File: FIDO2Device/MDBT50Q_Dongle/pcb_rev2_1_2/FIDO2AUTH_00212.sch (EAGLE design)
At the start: 39 parts, among them CN1 TE-1734028, CN2 IF_4PIN, CN5 IF_2PIN_SOL, SW1 SKRPACE010, SW2 SKTADAE010, U1 MDBT50Q-P1M, U2 XC6206P332MR-G, U3 ATECC608A-MAHDA-S, X1 NX3215SA-32.768K

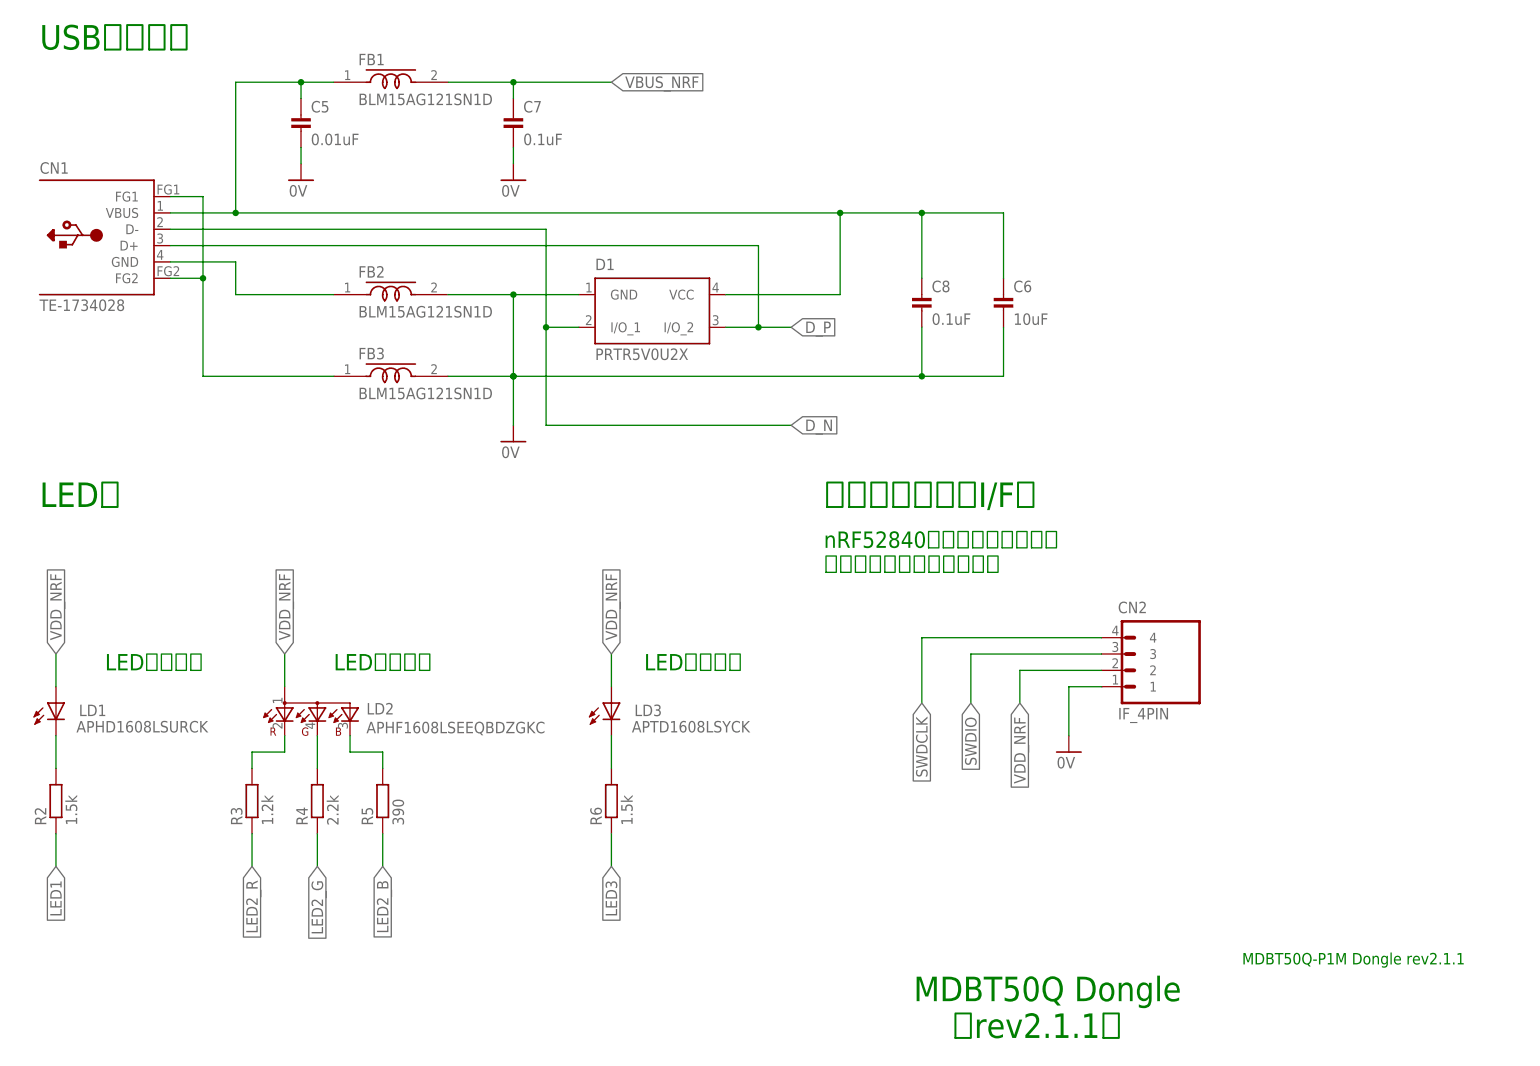
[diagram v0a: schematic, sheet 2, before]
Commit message: 回路図・レイアウトを修正
・３色LEDを単色LEDに分割
・LEDの部品番号を修正
・旧・LED1（赤色LED）は廃止
・配線／ビア位置を若干見直し
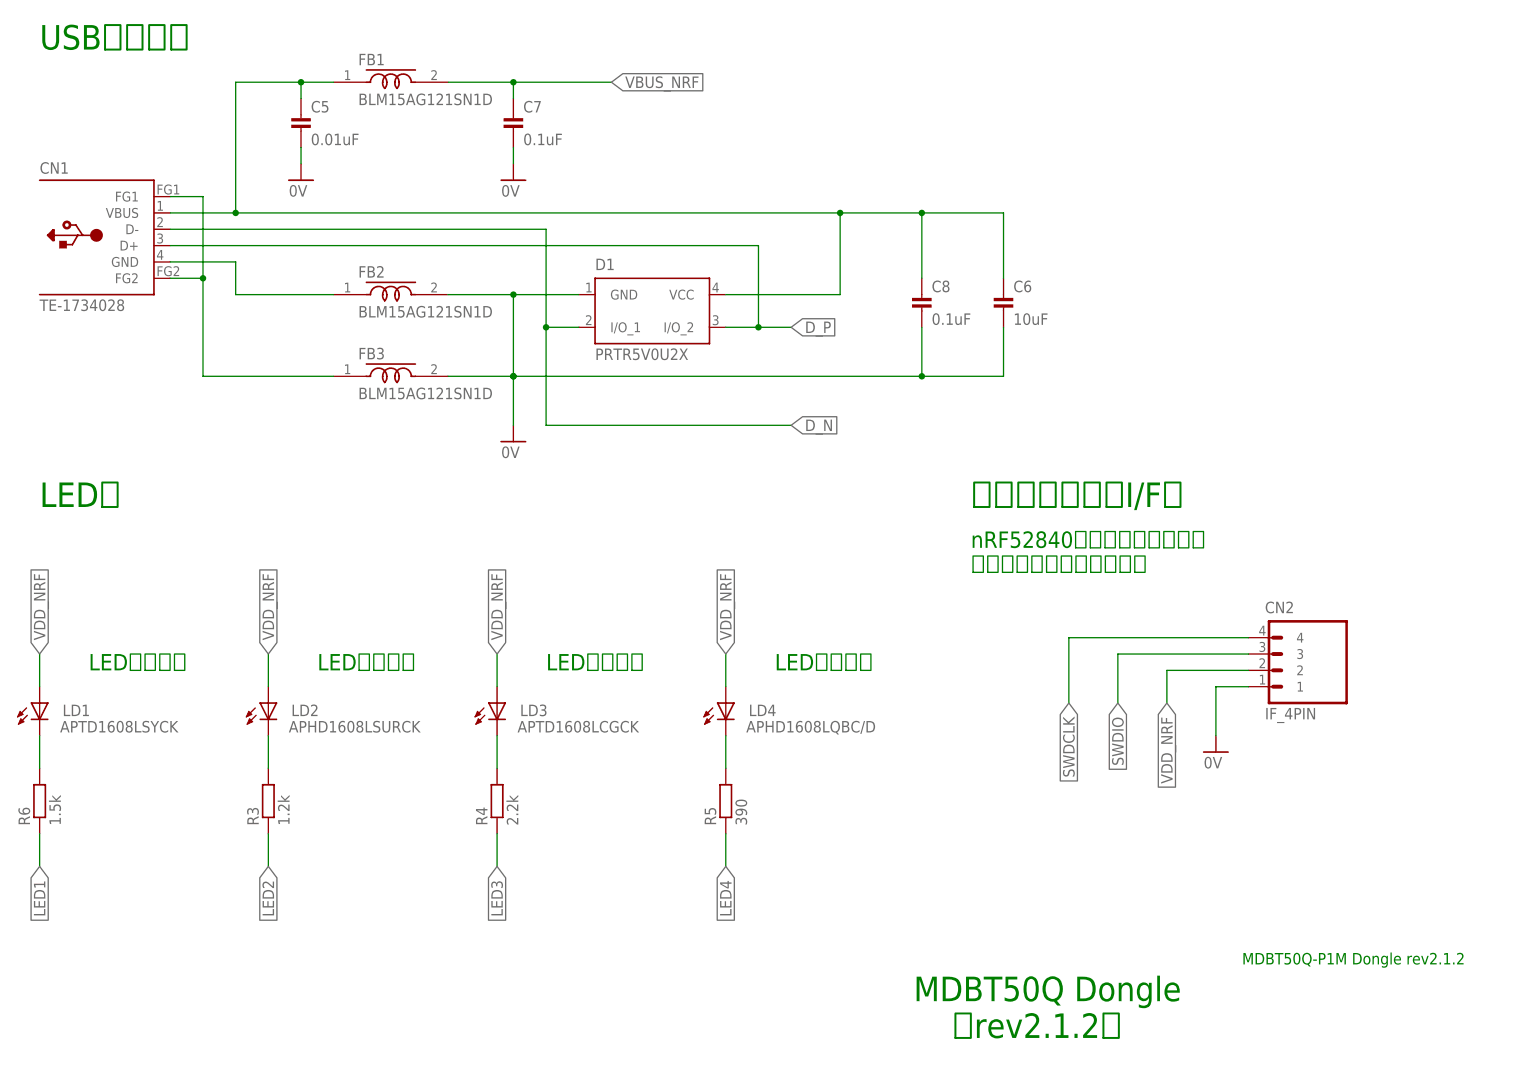
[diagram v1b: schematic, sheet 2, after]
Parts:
- removed R2: 1.5k, Parts:RESISTOR_0402
- added LD4: APHD1608LQBC/D, Parts:APHD1608LQBC/D
- LD1: value APHD1608LSURCK -> APTD1608LSYCK; device Parts:APHD1608LSURCK -> Parts:APTD1608LSYCK
- LD2: value APHF1608LSEEQBDZGKC -> APHD1608LSURCK; device Parts:APHF1608LSEEQBDZGKC -> Parts:APHD1608LSURCK
- LD3: value APTD1608LSYCK -> APTD1608LCGCK; device Parts:APTD1608LSYCK -> Parts:APTD1608LCGCK
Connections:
- net LED2_B renamed LED4
- net LED2_R renamed LED2
- removed net LED2_G: R4.1, U1.P1.09
- removed net N$11: LD1.C, R2.2
- net LED1: now also R6.1, U1.P0.26; no longer R2.1, U1.P0.27
- net LED3: now also R4.1, U1.P1.09; no longer R6.1, U1.P0.26
- net N$1: now also LD4.C, R5.2; no longer LD2.CRED, R3.2
- net N$6: now also LD3.C; no longer LD2.CGREEN
- net N$7: now also LD2.C, R3.2; no longer LD2.CBLUE, R5.2
- net N$8: now also LD1.C; no longer LD3.C
- net VDD_NRF: now also LD4.A
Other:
- note added: "LED（緑色）"
- note added: "LED（青色）"
- note added: "MDBT50Q Dongle （rev2.1.2）"
- note added: "MDBT50Q-P1M Dongle rev2.1.2"
- note removed: "LED（３色）"
- note removed: "MDBT50Q Dongle （rev2.1.1）"
- note removed: "MDBT50Q-P1M Dongle rev2.1.1"
- moved on the sheet: CN2, LD1, LD3, R3, R4, R5, R6

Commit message: 回路図・レイアウトを修正
・LED品番を、入手性の良い物に変更
・LED関連のレイアウトを修正（パターンを修正）
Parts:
- LD1: value APTD1608LSYCK -> APTD1608LSECK/J4-PF; device Parts:APTD1608LSYCK -> Parts:APTD1608LSECK/J4-PF
- LD3: value APTD1608LCGCK -> APTD1608LZGCK; device Parts:APTD1608LCGCK -> Parts:APTD1608LZGCK
- LD4: value APHD1608LQBC/D -> APTD1608LVBC/D; device Parts:APHD1608LQBC/D -> Parts:APTD1608LVBC/D
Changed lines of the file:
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@@
 <grid distance="0.1" unitdist="inch" unit="inch" style="lines" multiple="1" display="yes" altdistance="0.01" altunitdist="inch" altunit="inch"/>
 <layers>
-<layer number="1" name="Top" color="4" fill="1" visible="no" active="no"/>
-<layer number="2" name="Route2" color="1" fill="3" visible="no" active="no"/>
-<layer number="3" name="Route3" color="4" fill="3" visible="no" active="no"/>
-<layer number="14" name="Route14" color="1" fill="6" visible="no" active="no"/>
-<layer number="15" name="Route15" color="4" fill="6" visible="no" active="no"/>
-<layer number="16" name="Bottom" color="1" fill="1" visible="no" active="no"/>
-<layer number="17" name="Pads" color="2" fill="1" visible="no" active="no"/>
-<layer number="18" name="Vias" color="2" fill="1" visible="no" active="no"/>
-<layer number="19" name="Unrouted" color="6" fill="1" visible="no" active="no"/>
-<layer number="20" name="Dimension" color="15" fill="1" visible="no" active="no"/>
-<layer number="21" name="tPlace" color="7" fill="1" visible="no" active="no"/>
-<layer number="22" name="bPlace" color="7" fill="1" visible="no" active="no"/>
-<layer number="23" name="tOrigins" color="15" fill="1" visible="no" active="no"/>
-<layer number="24" name="bOrigins" color="15" fill="1" visible="no" active="no"/>
-<layer number="25" name="tNames" color="7" fill="1" visible="no" active="no"/>
-<layer number="26" name="bNames" color="7" fill="1" visible="no" active="no"/>
-<layer number="27" name="tValues" color="7" fill="1" visible="no" active="no"/>
-<layer number="28" name="bValues" color="7" fill="1" visible="no" active="no"/>
+<layer number="1" name="Top" color="4" fill="1" visible="yes" active="no"/>
+<layer number="2" name="Route2" color="1" fill="3" visible="yes" active="no"/>
+<layer number="3" name="Route3" color="4" fill="3" visible="yes" active="no"/>
+<layer number="14" name="Route14" color="1" fill="6" visible="yes" active="no"/>
+<layer number="15" name="Route15" color="4" fill="6" visible="yes" active="no"/>
+<layer number="16" name="Bottom" color="1" fill="1" visible="yes" active="no"/>
+<layer number="17" name="Pads" color="2" fill="1" visible="yes" active="no"/>
+<layer number="18" name="Vias" color="2" fill="1" visible="yes" active="no"/>
+<layer number="19" name="Unrouted" color="6" fill="1" visible="yes" active="no"/>
+<layer number="20" name="Dimension" color="15" fill="1" visible="yes" active="no"/>
+<layer number="21" name="tPlace" color="7" fill="1" visible="yes" active="no"/>
+<layer number="22" name="bPlace" color="7" fill="1" visible="yes" active="no"/>
+<layer number="23" name="tOrigins" color="15" fill="1" visible="yes" active="no"/>
+<layer number="24" name="bOrigins" color="15" fill="1" visible="yes" active="no"/>
+<layer number="25" name="tNames" color="7" fill="1" visible="yes" active="no"/>
+<layer number="26" name="bNames" color="7" fill="1" visible="yes" active="no"/>
+<layer number="27" name="tValues" color="7" fill="1" visible="yes" active="no"/>
+<layer number="28" name="bValues" color="7" fill="1" visible="yes" active="no"/>
 <layer number="29" name="tStop" color="7" fill="3" visible="no" active="no"/>
 <layer number="30" name="bStop" color="7" fill="6" visible="no" active="no"/>
@@
 <layer number="35" name="tGlue" color="7" fill="4" visible="no" active="no"/>
 <layer number="36" name="bGlue" color="7" fill="5" visible="no" active="no"/>
-<layer number="37" name="tTest" color="7" fill="1" visible="no" active="no"/>
-<layer number="38" name="bTest" color="7" fill="1" visible="no" active="no"/>
+<layer number="37" name="tTest" color="7" fill="1" visible="yes" active="no"/>
+<layer number="38" name="bTest" color="7" fill="1" visible="yes" active="no"/>
 <layer number="39" name="tKeepout" color="4" fill="11" visible="no" active="no"/>
 <layer number="40" name="bKeepout" color="1" fill="11" visible="no" active="no"/>
@@
 <layer number="44" name="Drills" color="7" fill="1" visible="no" active="no"/>
 <layer number="45" name="Holes" color="7" fill="1" visible="no" active="no"/>
-<layer number="46" name="Milling" color="3" fill="1" visible="no" active="no"/>
-<layer number="47" name="Measures" color="7" fill="1" visible="no" active="no"/>
-<layer number="48" name="Document" color="7" fill="1" visible="no" active="no"/>
-<layer number="49" name="Reference" color="7" fill="1" visible="no" active="no"/>
-<layer number="50" name="dxf" color="7" fill="1" visible="no" active="no"/>
-<layer number="51" name="tDocu" color="7" fill="1" visible="no" active="no"/>
-<layer number="52" name="bDocu" color="7" fill="1" visible="no" active="no"/>
-<layer number="53" name="tGND_GNDA" color="7" fill="9" visible="no" active="no"/>
-<layer number="54" name="bGND_GNDA" color="1" fill="9" visible="no" active="no"/>
-<layer number="56" name="wert" color="7" fill="1" visible="no" active="no"/>
-<layer number="57" name="tCAD" color="7" fill="1" visible="no" active="no"/>
-<layer number="59" name="tCarbon" color="7" fill="1" visible="no" active="no"/>
-<layer number="60" name="bCarbon" color="7" fill="1" visible="no" active="no"/>
+<layer number="46" name="Milling" color="3" fill="1" visible="yes" active="no"/>
+<layer number="47" name="Measures" color="7" fill="1" visible="yes" active="no"/>
+<layer number="48" name="Document" color="7" fill="1" visible="yes" active="no"/>
+<layer number="49" name="Reference" color="7" fill="1" visible="yes" active="no"/>
+<layer number="50" name="dxf" color="7" fill="1" visible="yes" active="no"/>
+<layer number="51" name="tDocu" color="7" fill="1" visible="yes" active="no"/>
+<layer number="52" name="bDocu" color="7" fill="1" visible="yes" active="no"/>
+<layer number="53" name="tGND_GNDA" color="7" fill="9" visible="yes" active="no"/>
+<layer number="54" name="bGND_GNDA" color="1" fill="9" visible="yes" active="no"/>
+<layer number="56" name="wert" color="7" fill="1" visible="yes" active="no"/>
+<layer number="57" name="tCAD" color="7" fill="1" visible="yes" active="no"/>
+<layer number="59" name="tCarbon" color="7" fill="1" visible="yes" active="no"/>
+<layer number="60" name="bCarbon" color="7" fill="1" visible="yes" active="no"/>
 <layer number="90" name="Modules" color="5" fill="1" visible="yes" active="yes"/>
 <layer number="91" name="Nets" color="2" fill="1" visible="yes" active="yes"/>
@@
 <part name="BAT1" library="Connectors" deviceset="BAT-HLD-012-SMT" device=""/>
 <part name="GND18" library="Supply" deviceset="0V" device=""/>
-<part name="LD1" library="Parts" deviceset="APTD1608" device="LSYCK"/>
+<part name="LD1" library="Parts" deviceset="APTD1608" device="LSECK/J4-PF" value="APTD1608LSECK/J4-PF"/>
 <part name="R6" library="Parts" deviceset="RESISTOR" device="_0402" value="1.5k"/>
 <part name="FRAME4" library="Generic" deviceset="A4L-LOC" device=""/>
@@
 <part name="R7" library="Parts" deviceset="RESISTOR" device="_0402" value="3.6k"/>
 <part name="R8" library="Parts" deviceset="RESISTOR" device="_0402" value="3.6k"/>
-<part name="LD3" library="Parts" deviceset="APTD1608" device="LCGCK"/>
+<part name="LD3" library="Parts" deviceset="APTD1608" device="LZGCK" value="APTD1608LZGCK"/>
 <part name="LD2" library="Parts" deviceset="APHD1608" device="LSURCK"/>
-<part name="LD4" library="Parts" deviceset="APHD1608" device="LQBC/D"/>
+<part name="LD4" library="Parts" deviceset="APTD1608" device="LVBC/D"/>
 </parts>
 <sheets>
